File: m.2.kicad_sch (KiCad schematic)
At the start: 29 parts, among them CN9 DF40C-40DP-0.4V, J9 Bus_M.2_Socket_B, U44 TS5A23157DGSR, U45 TS5A23157DGSR, U46 TS5A23157DGSR, U53 NANO SIM 7P 1.37H PUSH, U54 SiP32508DT, U64 TF PUSH

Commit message: imported footprints and 3d models, replaced obsolete components, finished schematic audit, wired new usb hub and flash chip + more, removed stale nets
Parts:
- removed R76: 47kΩ, Resistor_SMD:R_0603_1608Metric, symbol Device:R_Small
- removed U53: NANO SIM 7P 1.37H PUSH, symbol slate113:NANO-SIM-7P-1.37H-PUSH
- removed U64: TF PUSH, symbol slate113:TF-PUSH
- added Card1: NANO SIM 7P 1.37H PUSH, slate113:SIM-SMD_YKSIM-PUSH137-140NANO, symbol slate113:NANOSIM7P1.37HPUSH
- added Card2: TF PUSH, slate113:TF-SMD_TF-PUSH, symbol slate113:TFPUSH
- added R26, R38: 47kΩ, Resistor_SMD:R_0603_1608Metric, symbol Device:R_Small
- R62, R63: LCSC Part C23162 -> C163914; MPN 0603WAF4701T5E -> WR06X4701FTL; Manufacturer Yageo -> Walsin
- R64: LCSC Part C25804 -> C840630; MPN 0603WAF1002T5E -> CR0603-FX-1002ELF; Manufacturer Yageo -> Bourns
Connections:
- net GND: now also Card1.C5 (GND), Card2.10, Card2.11, Card2.12, Card2.13, Card2.6 (VSS)
- net MODEM_W_DISABLE: now also CN9.36
- net PCIE0_RXN: now also J9.47 (PETn0/SATA-A-)
- net PCIE0_RXP: now also J9.49 (PETp0/SATA-A+)
- net PCIE0_TXN: now also J9.41 (PERn0/SATA-B+); no longer J9.47 (PETn0/SATA-A-)
- net PCIE0_TXP: now also J9.43 (PERp0/SATA-B-); no longer J9.49 (PETp0/SATA-A+)
- net PCIE0_WAKE: now also CN9.35
- net SD_CLK: now also Card2.5 (CLX)
- net SD_CMD: now also Card2.3 (CMD)
- net SD_D0: now also Card2.8 (DAT1)
- net SD_D1: now also Card2.7 (DAT0)
- net SD_D2: now also Card2.1 (DAT2)
- net SD_D3: now also Card2.2 (CD/DAT3)
- net SD_DET: now also Card2.CD, R38.1; no longer J9.40 (GPIO_0), J9.66 (SIM_DETECT)
- net SD_VDD: now also Card2.4 (VDD), R38.2
- net USIM1_CLK: now also Card1.C3 (CLK)
- net USIM1_DATA: now also Card1.C7 (I/O)
- net USIM1_PWR: now also Card1.C1 (VCC), R26.2
- net USIM1_RST: now also Card1.C2 (RST)
- net USIM2_CLK: no longer names the net of J9.44 (GPIO_2)
- net USIM2_DATA: no longer names the net of J9.42 (GPIO_1)
- net USIM2_PWR: no longer names the net of J9.48 (GPIO_4)
- net USIM2_RST: no longer names the net of J9.46 (GPIO_3)
- new net SIM_DET: Card1.CD (DETECT-SWITCH), J9.66 (SIM_DETECT), R26.1
- no-connect marks 31 -> 37
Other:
- note added: "SIM + SD Card Slot"
- note removed: "SIM x2 + SD Card Slot"

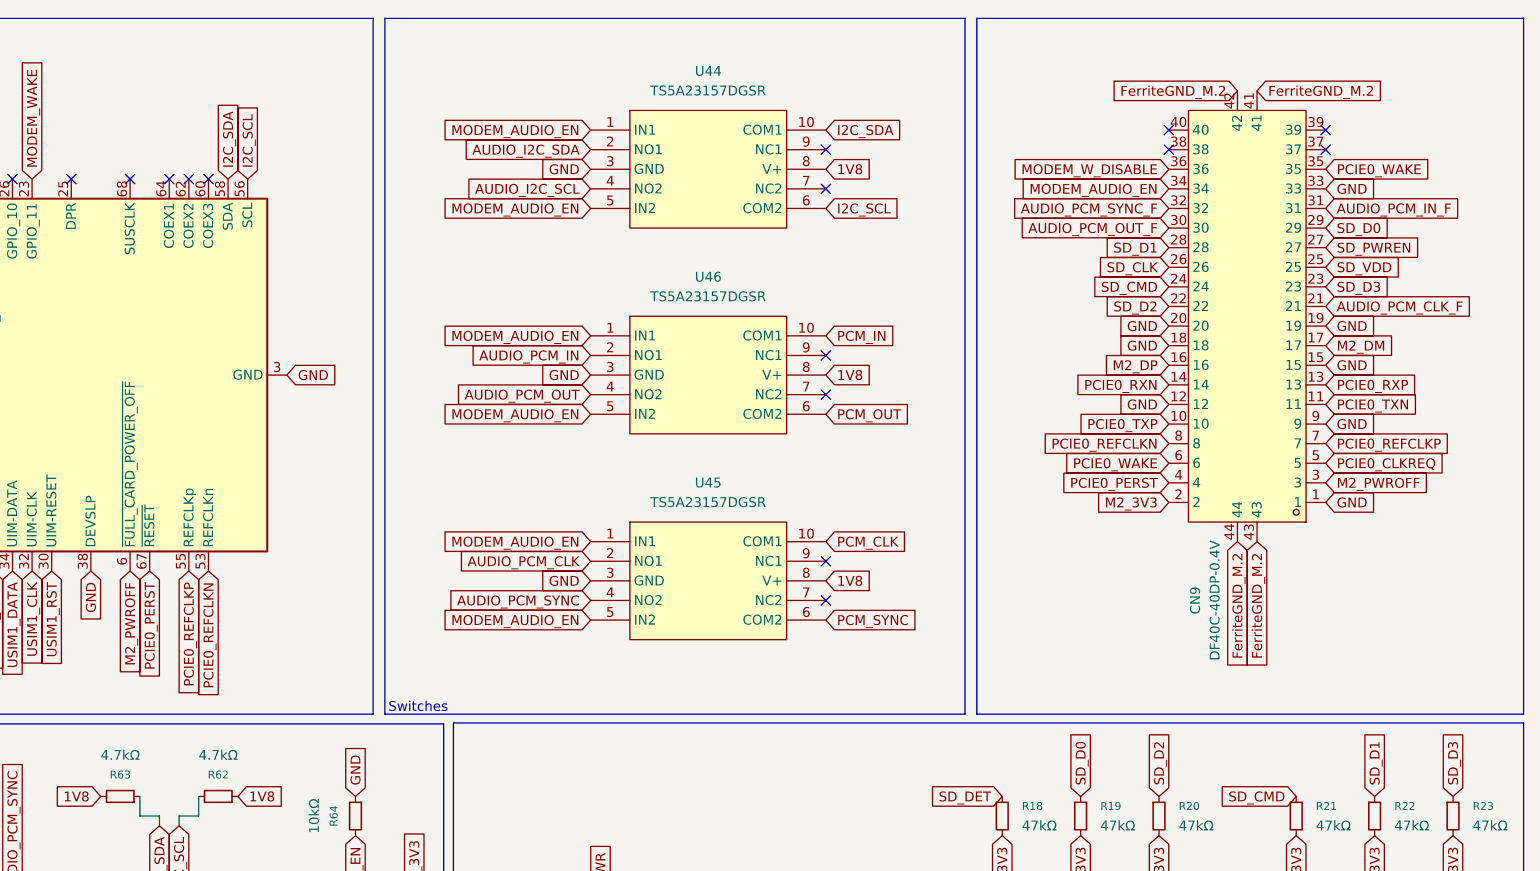
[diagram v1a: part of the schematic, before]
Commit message: continued work on carrier board, started work on m.2 board
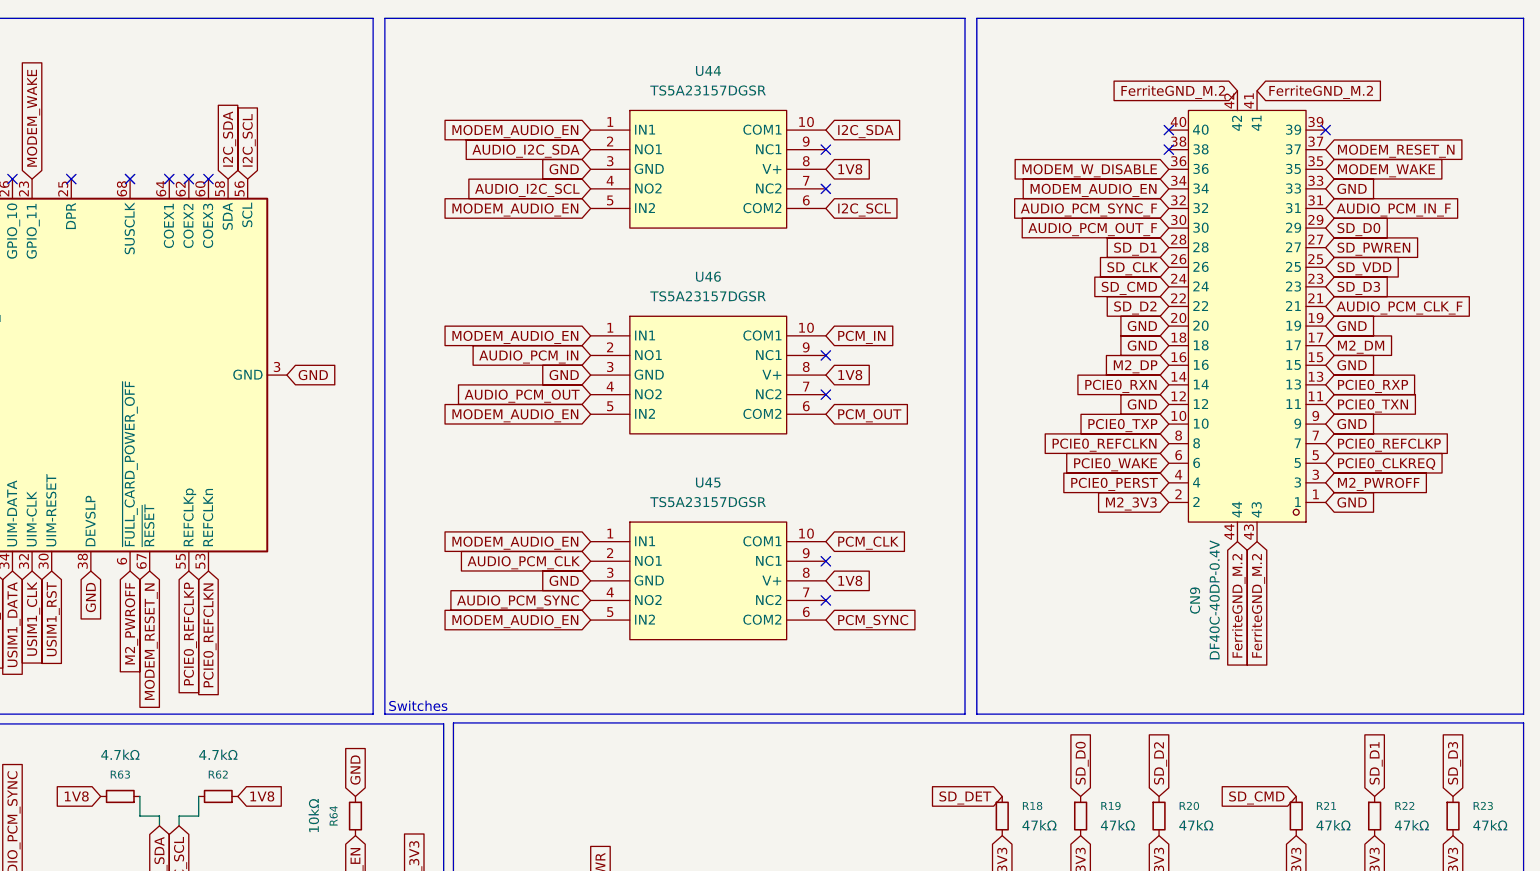
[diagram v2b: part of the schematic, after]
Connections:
- net MODEM_WAKE: now also CN9.35
- net PCIE0_PERST: no longer J9.67 (~{RESET})
- net PCIE0_WAKE: no longer CN9.35
- net MODEM_RESET_N: now reaches CN9.37
- net MODEM_RESET_N: now also J9.67 (~{RESET})
- no-connect marks 37 -> 36
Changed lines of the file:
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@@
 	)
 	(no_connect
-		(at 257.81 30.48)
-	)
-	(no_connect
 		(at 107.95 34.29)
 	)
@@
 		)
 	)
+	(global_label "MODEM_WAKE"
+		(shape input)
+		(at 257.81 33.02 0)
+		(fields_autoplaced yes)
+		(effects
+			(font
+				(size 1.27 1.27)
+			)
+			(justify left)
+		)
+		(property "Intersheetrefs" "${INTERSHEET_REFS}"
+			(at 273.3741 33.02 0)
+			(hide yes)
+			(show_name no)
+			(do_not_autoplace no)
+			(effects
+				(font
+					(size 1.27 1.27)
+				)
+				(justify left)
+			)
+		)
+	)
 	(global_label "AUDIO_I2C_SCL"
 		(shape input)
@@
 		)
 	)
+	(global_label "MODEM_RESET_N"
+		(shape input)
+		(at 257.81 30.48 0)
+		(fields_autoplaced yes)
+		(effects
+			(font
+				(size 1.27 1.27)
+			)
+			(justify left)
+		)
+		(property "Intersheetrefs" "${INTERSHEET_REFS}"
+			(at 276.4583 30.48 0)
+			(hide yes)
+			(show_name no)
+			(do_not_autoplace no)
+			(effects
+				(font
+					(size 1.27 1.27)
+				)
+				(justify left)
+			)
+		)
+	)
 	(global_label "3V3"
 		(shape input)
@@
 		)
 	)
-	(global_label "PCIE0_PERST"
+	(global_label "MODEM_RESET_N"
 		(shape input)
 		(at 105.41 85.09 270)
@@
 		)
 		(property "Intersheetrefs" "${INTERSHEET_REFS}"
-			(at 105.41 100.4122 90)
+			(at 105.41 103.7383 90)
 			(hide yes)
 			(show_name no)
@@
 			)
 		)
-	)
-	(global_label "PCIE0_WAKE"
-		(shape input)
-		(at 257.81 33.02 0)
-		(fields_autoplaced yes)
-		(effects
-			(font
-				(size 1.27 1.27)
-			)
-			(justify left)
-		)
-		(property "Intersheetrefs" "${INTERSHEET_REFS}"
-			(at 272.2251 33.02 0)
-			(hide yes)
-			(show_name no)
-			(do_not_autoplace no)
-			(effects
-				(font
-					(size 1.27 1.27)
-				)
-				(justify left)
-			)
-		)

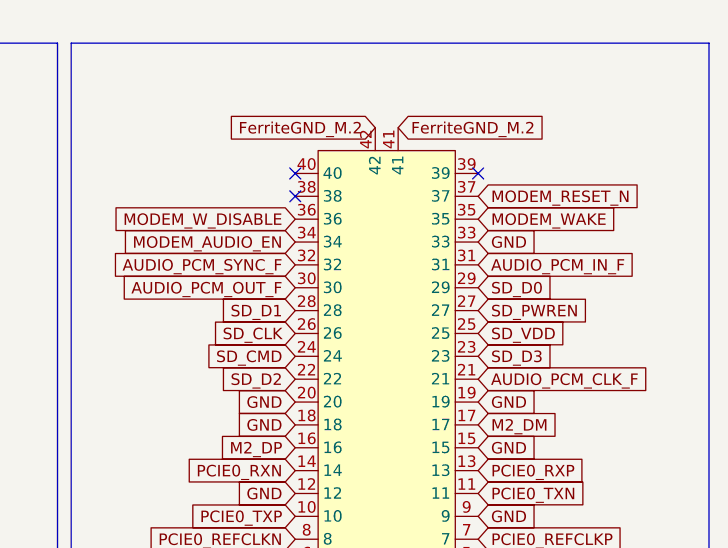
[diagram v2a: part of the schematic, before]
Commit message: finished m.2 board and copper pours, completed antenna bracket and power board, finished slateconnect board, reorganized libraries
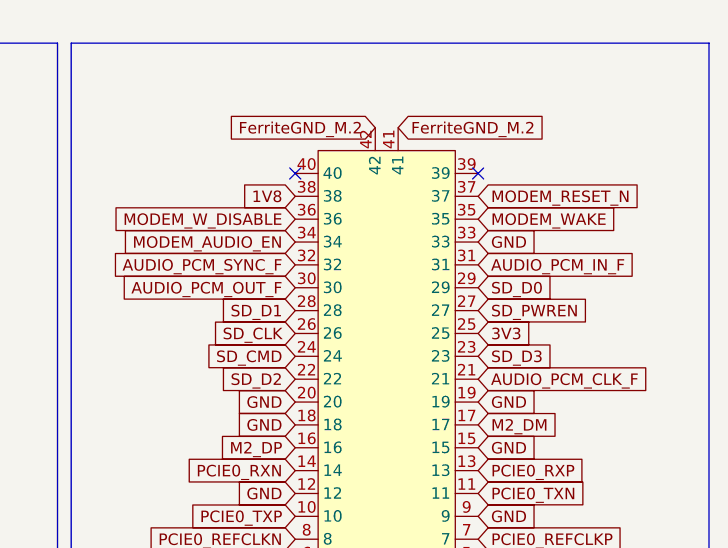
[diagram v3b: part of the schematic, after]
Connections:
- net 1V8: now also CN9.38
- net 3V3: now also CN9.25
- net SD_VDD: no longer CN9.25
- no-connect marks 36 -> 35
